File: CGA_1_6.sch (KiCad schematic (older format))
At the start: 10 parts, among them U50 2118, U51 2118, U52 2118, U53 2118, U54 2118, U55 2118, U56 2118, U57 2118, U60 74LS374, U61 74LS374

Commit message: Complete a sheet
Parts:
- added U13: 74LS08, Package_DIP:DIP-14_W7.62mm_LongPads, symbol 74xx:74LS08
- added U14: 74LS32, Package_DIP:DIP-14_W7.62mm_LongPads, symbol 74xx:74LS32
- added U28: 74LS10, Package_DIP:DIP-14_W7.62mm_LongPads, symbol 74xx:74LS10
- added U38: MC6845, Package_DIP:DIP-40_W15.24mm_LongPads, symbol GPU:MC6845
- added U48: 74LS51, Package_DIP:DIP-14_W7.62mm_LongPads, symbol 74xx:74LS51
- added U49: 74LS02, symbol 74xx:74LS02
- added U58, U59: 74LS374, Package_DIP:DIP-20_W7.62mm_LongPads, symbol 74xx:74LS374
- added U62: 74LS125, Package_DIP:DIP-14_W10.16mm_LongPads, symbol 74xx:74LS125
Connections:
- net A0: now also U38.24 (RS), U58.2 (O0), U59.2 (O0)
- net A1: now also U58.5 (O1), U59.5 (O1)
- net A2: now also U58.6 (O2), U59.6 (O2)
- net A3: now also U58.9 (O3), U59.9 (O3)
- net A4: now also U58.12 (O4), U59.12 (O4)
- net A5: now also U59.15 (O5), U62.3
- net A6: now also U58.15 (O5), U59.16 (O6)
- net GND: now also U38.1 (GND), U58.10 (GND), U59.10 (GND)
- net VCC: now also U38.20 (VCC), U48.10, U48.13, U58.20 (VCC), U59.20 (VCC)
- net ~RAS: now also U58.11 (Cp), U59.11 (Cp)
- new net: U14.5, U49.13
- new net: U13.11, U14.4
- new net: U13.12, U14.3
- new net: U14.1, U28.8
- new net: U38.8 (MA4), U59.13 (D4)
- new net: U38.9 (MA5), U59.14 (D5)
- new net: U38.10 (MA6), U59.17 (D6)
- new net: U38.4 (MA0), U59.3 (D0)
- new net: U38.5 (MA1), U59.4 (D1)
- new net: U38.6 (MA2), U59.7 (D2)
- new net: U38.7 (MA3), U59.8 (D3)
- new net: U38.15 (MA11), U58.13 (D4)
- new net: U49.10, U58.14 (D5)
- new net: U38.11 (MA7), U58.3 (D0)
- new net: U38.12 (MA8), U58.4 (D1)
- new net: U38.13 (MA9), U58.7 (D2)
- new net: U38.14 (MA10), U58.8 (D3)
- new net: U48.8, U49.8, U49.9
- new net: U38.16 (MA12), U48.9
- new net ALPHA_DOTS: U14.6
- new net AT7: U28.11
- new net CHG_DOTS: U13.13
- new net CURSOR: U38.19 (CURSOR)
- new net D0: U38.33 (D0)
- new net D1: U38.32 (D1)
- new net D2: U38.31 (D2)
- new net D3: U38.30 (D3)
- new net D4: U38.29 (D4)
- new net D5: U38.28 (D5)
- new net D6: U38.27 (D6)
- new net D7: U38.26 (D7)
- new net DISPEN: U38.18 (DE)
- new net E: U38.23 (E)
- new net ENABLE_BLINK: U28.10
- new net GRPH: U48.12
- new net HSYNC: U38.39 (HS)
- new net LPEN_STR: U38.3 (LPSTB)
- new net RA0: U38.38 (RA0), U48.1
- new net RA1: U38.37 (RA1)
- new net RA2: U38.36 (RA2)
- new net VSYNC: U38.40 (VS)
- new net ~6845_CS: U38.25 (~CS)
- new net ~BLINK: U14.2
- new net ~CCLK: U38.21 (CLK)
- new net ~CURSOR_BLINK: U49.12
- new net ~CURSOR_DLY: U28.9, U49.11
- new net ~EN_CRT_CAS_ADDR: U58.1 (OE), U62.1
- new net ~EN_CRT_RAS_ADDR: U59.1 (OE)
- new net ~GRPH: U48.11
- new net ~HCLK: U62.2
- new net ~IOW: U38.22 (R/~W)
- new net ~RESET: U38.2 (~RESET)
- no-connect marks 4 -> 13

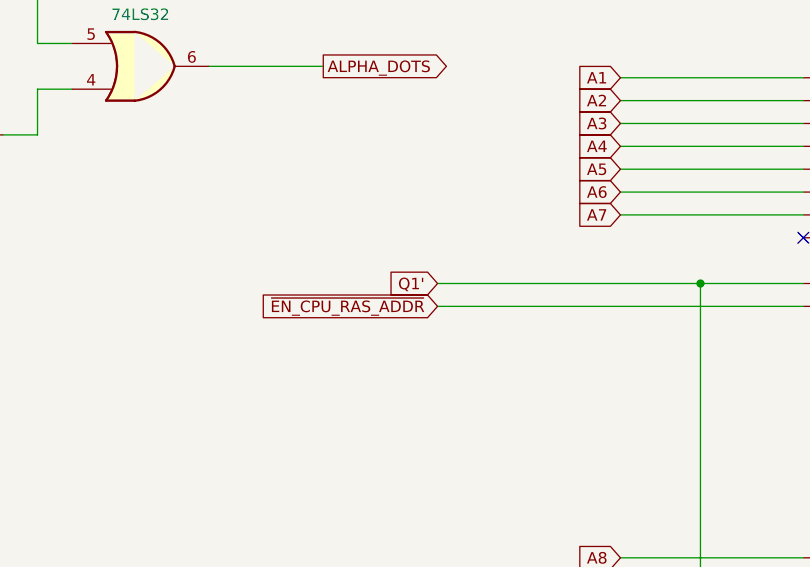
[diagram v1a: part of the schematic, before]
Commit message: Remove char from label
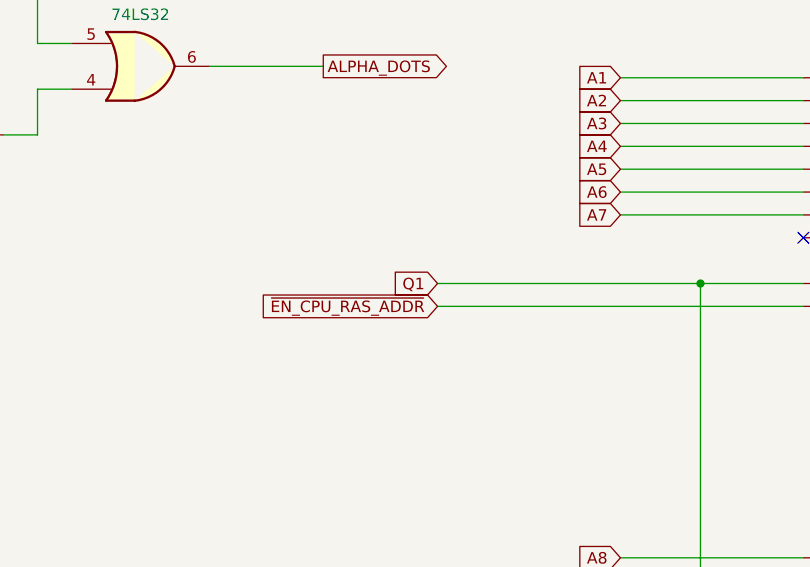
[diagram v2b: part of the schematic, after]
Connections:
- net Q1' renamed Q1
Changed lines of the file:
@@
 Connection ~ 7700 2300
 Text GLabel 6550 2300 0    50   Input ~ 0
-Q1'
+Q1
 Wire Wire Line
 	8150 2400 6550 2400
